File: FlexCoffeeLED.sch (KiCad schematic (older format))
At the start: 29 parts, among them IC1 LM75BDP,118, IC2 PIC16F18426-I_ST, IC3 LM75BDP,118, IC4 LM75BDP,118, J1 Conn_01x05_Male, J2 Conn_01x03_Male, J3 Conn_01x03_Male

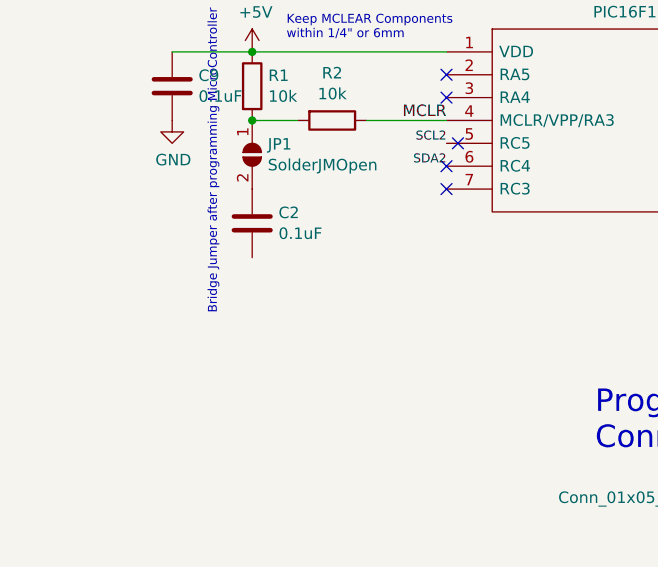
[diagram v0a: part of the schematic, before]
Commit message: Added .git attributes Routed New PCB Design Passed DRC.
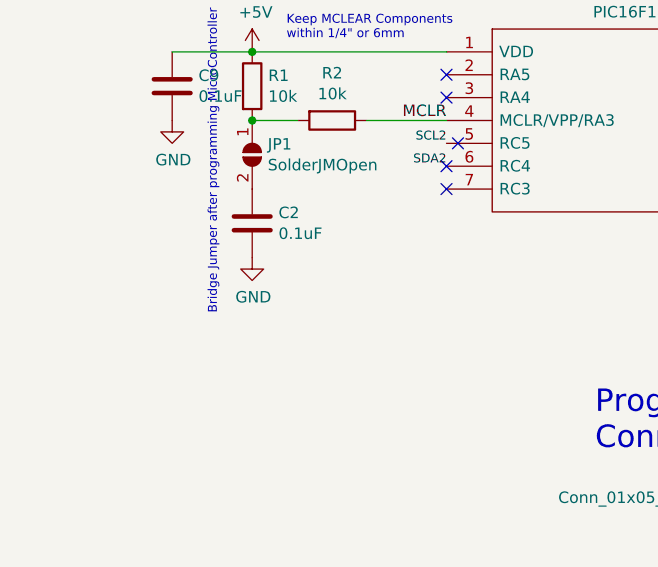
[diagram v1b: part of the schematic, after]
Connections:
- net GND: now also C2.2
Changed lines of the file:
@@
 $EndComp
 $Comp
-L power:+5V #PWR0102
+L power:+5V #PWR?
 U 1 1 5CAA0C63
 P 1650 1100
-F 0 "#PWR0102" H 1650 950 50  0001 C CNN
+F 0 "#PWR?" H 1650 950 50  0001 C CNN
 F 1 "+5V" H 1665 1273 50  0000 C CNN
 F 2 "" H 1650 1100 50  0001 C CNN
@@
 $EndComp
 $Comp
-L power:+5V #PWR0103
+L power:+5V #PWR?
 U 1 1 5CAA255E
 P 2800 1200
-F 0 "#PWR0103" H 2800 1050 50  0001 C CNN
+F 0 "#PWR?" H 2800 1050 50  0001 C CNN
 F 1 "+5V" H 2815 1373 50  0000 C CNN
 F 2 "" H 2800 1200 50  0001 C CNN
@@
 	2800 1350 2800 1200
 $Comp
-L power:GND #PWR0107
+L power:GND #PWR?
 U 1 1 5CAA5599
 P 2450 1450
-F 0 "#PWR0107" H 2450 1200 50  0001 C CNN
+F 0 "#PWR?" H 2450 1200 50  0001 C CNN
 F 1 "GND" H 2455 1277 50  0000 C CNN
 F 2 "" H 2450 1450 50  0001 C CNN
@@
 $EndComp
 $Comp
-L power:GND #PWR0108
+L power:GND #PWR?
 U 1 1 5CAA5C01
 P 3600 1450
-F 0 "#PWR0108" H 3600 1200 50  0001 C CNN
+F 0 "#PWR?" H 3600 1200 50  0001 C CNN
 F 1 "GND" H 3605 1277 50  0000 C CNN
 F 2 "" H 3600 1450 50  0001 C CNN
@@
 SDA_5V
 $Comp
-L power:GND #PWR0111
+L power:GND #PWR?
 U 1 1 5CAACCDF
 P 5150 4250
-F 0 "#PWR0111" H 5150 4000 50  0001 C CNN
+F 0 "#PWR?" H 5150 4000 50  0001 C CNN
 F 1 "GND" H 5155 4077 50  0000 C CNN
 F 2 "" H 5150 4250 50  0001 C CNN
@@
 PGC
 $Comp
-L power:GND #PWR0112
+L power:GND #PWR?
 U 1 1 5CAB3C4D
 P 4250 6550
-F 0 "#PWR0112" H 4250 6300 50  0001 C CNN
+F 0 "#PWR?" H 4250 6300 50  0001 C CNN
 F 1 "GND" H 4255 6377 50  0000 C CNN
 F 2 "" H 4250 6550 50  0001 C CNN
@@
 $EndComp
 $Comp
-L power:+5V #PWR0113
+L power:+5V #PWR?
 U 1 1 5CAB40F3
 P 4250 6300
-F 0 "#PWR0113" H 4250 6150 50  0001 C CNN
+F 0 "#PWR?" H 4250 6150 50  0001 C CNN
 F 1 "+5V" H 4265 6473 50  0000 C CNN
 F 2 "" H 4250 6300 50  0001 C CNN
@@
 	2750 1450 2800 1450
 $Comp
-L power:GND #PWR0118
+L power:GND #PWR?
 U 1 1 5CAE2ED7
 P 2750 1750
-F 0 "#PWR0118" H 2750 1500 50  0001 C CNN
+F 0 "#PWR?" H 2750 1500 50  0001 C CNN
 F 1 "GND" H 2755 1577 50  0000 C CNN
 F 2 "" H 2750 1750 50  0001 C CNN
@@
 $EndComp
 $Comp
-L power:GND #PWR0120
+L power:GND #PWR?
 U 1 1 5CAE8A3F
 P 1550 1750
-F 0 "#PWR0120" H 1550 1500 50  0001 C CNN
+F 0 "#PWR?" H 1550 1500 50  0001 C CNN
 F 1 "GND" H 1555 1577 50  0000 C CNN
 F 2 "" H 1550 1750 50  0001 C CNN
@@
 $EndComp
 $Comp
-L power:GND #PWR0122
+L power:GND #PWR?
 U 1 1 5CB06AB4
 P 1600 4550
-F 0 "#PWR0122" H 1600 4300 50  0001 C CNN
+F 0 "#PWR?" H 1600 4300 50  0001 C CNN
 F 1 "GND" H 1605 4377 50  0000 C CNN
 F 2 "" H 1600 4550 50  0001 C CNN
@@
 $EndComp
 $Comp
-L power:+5V #PWR0123
+L power:+5V #PWR?
 U 1 1 5CB1B5D7
 P 1950 4250
-F 0 "#PWR0123" H 1950 4100 50  0001 C CNN
+F 0 "#PWR?" H 1950 4100 50  0001 C CNN
 F 1 "+5V" H 1965 4423 50  0000 C CNN
 F 2 "" H 1950 4250 50  0001 C CNN
@@
 $EndComp
 $Comp
-L power:+5V #PWR0101
+L power:+5V #PWR?
 U 1 1 5CBD0BE3
 P 9750 4250
-F 0 "#PWR0101" H 9750 4100 50  0001 C CNN
+F 0 "#PWR?" H 9750 4100 50  0001 C CNN
 F 1 "+5V" H 9765 4423 50  0000 C CNN
 F 2 "" H 9750 4250 50  0001 C CNN
@@
 $EndComp
 $Comp
-L power:GND #PWR0104
+L power:GND #PWR?
 U 1 1 5CBD0BF0
 P 9750 4650
-F 0 "#PWR0104" H 9750 4400 50  0001 C CNN
+F 0 "#PWR?" H 9750 4400 50  0001 C CNN
 F 1 "GND" H 9755 4477 50  0000 C CNN
 F 2 "" H 9750 4650 50  0001 C CNN
@@
 	9050 4350 9750 4350
 $Comp
-L power:+5V #PWR0106
+L power:+5V #PWR?
 U 1 1 5CBD1C72
 P 9750 5050
-F 0 "#PWR0106" H 9750 4900 50  0001 C CNN
+F 0 "#PWR?" H 9750 4900 50  0001 C CNN
 F 1 "+5V" H 9765 5223 50  0000 C CNN
 F 2 "" H 9750 5050 50  0001 C CNN
@@
 $EndComp
 $Comp
-L power:GND #PWR0109
+L power:GND #PWR?
 U 1 1 5CBD1C7F
 P 9750 5450
-F 0 "#PWR0109" H 9750 5200 50  0001 C CNN
+F 0 "#PWR?" H 9750 5200 50  0001 C CNN
 F 1 "GND" H 9755 5277 50  0000 C CNN
 F 2 "" H 9750 5450 50  0001 C CNN
@@
 	9050 5150 9350 5150
 $Comp
-L power:+5V #PWR0114
+L power:+5V #PWR?
 U 1 1 5CBD3265
 P 9750 5850
-F 0 "#PWR0114" H 9750 5700 50  0001 C CNN
+F 0 "#PWR?" H 9750 5700 50  0001 C CNN
 F 1 "+5V" H 9765 6023 50  0000 C CNN
 F 2 "" H 9750 5850 50  0001 C CNN
@@
 $EndComp
 $Comp
-L power:GND #PWR0115
+L power:GND #PWR?
 U 1 1 5CBD3272
 P 9750 6250
-F 0 "#PWR0115" H 9750 6000 50  0001 C CNN
+F 0 "#PWR?" H 9750 6000 50  0001 C CNN
 F 1 "GND" H 9755 6077 50  0000 C CNN
 F 2 "" H 9750 6250 50  0001 C CNN
@@
 Connection ~ 9050 4850
 $Comp
-L power:GND #PWR0116
+L power:GND #PWR?
 U 1 1 5CBDC4A5
 P 9400 4800
-F 0 "#PWR0116" H 9400 4550 50  0001 C CNN
+F 0 "#PWR?" H 9400 4550 50  0001 C CNN
 F 1 "GND" H 9405 4627 50  0000 C CNN
 F 2 "" H 9400 4800 50  0001 C CNN
@@
 	9050 4700 9400 4700
 $Comp
-L power:GND #PWR0117
+L power:GND #PWR?
 U 1 1 5CBDF46A
 P 9400 4000
-F 0 "#PWR0117" H 9400 3750 50  0001 C CNN
+F 0 "#PWR?" H 9400 3750 50  0001 C CNN
 F 1 "GND" H 9405 3827 50  0000 C CNN
 F 2 "" H 9400 4000 50  0001 C CNN
@@
 	9050 3900 9400 3900
 $Comp
-L power:GND #PWR0119
+L power:GND #PWR?
 U 1 1 5CBE0081
 P 9100 6300
-F 0 "#PWR0119" H 9100 6050 50  0001 C CNN
+F 0 "#PWR?" H 9100 6050 50  0001 C CNN
 F 1 "GND" H 9105 6127 50  0000 C CNN
 F 2 "" H 9100 6300 50  0001 C CNN
@@
 	9050 4150 9050 4250
 $Comp
-L power:GND #PWR0121
+L power:GND #PWR?
 U 1 1 5CBED2F8
 P 8050 4350
-F 0 "#PWR0121" H 8050 4100 50  0001 C CNN
+F 0 "#PWR?" H 8050 4100 50  0001 C CNN
 F 1 "GND" H 8055 4177 50  0000 C CNN
 F 2 "" H 8050 4350 50  0001 C CNN
@@
 $EndComp
 $Comp
-L power:GND #PWR0125
+L power:GND #PWR?
 U 1 1 5CBED88D
 P 8050 5150
-F 0 "#PWR0125" H 8050 4900 50  0001 C CNN
+F 0 "#PWR?" H 8050 4900 50  0001 C CNN
 F 1 "GND" H 8055 4977 50  0000 C CNN
 F 2 "" H 8050 5150 50  0001 C CNN
@@
 $EndComp
 $Comp
-L power:GND #PWR0126
+L power:GND #PWR?
 U 1 1 5CBEDD70
 P 8050 5950
-F 0 "#PWR0126" H 8050 5700 50  0001 C CNN
+F 0 "#PWR?" H 8050 5700 50  0001 C CNN
 F 1 "GND" H 8055 5777 50  0000 C CNN
 F 2 "" H 8050 5950 50  0001 C CNN
@@
 $EndComp
 $Comp
-L power:+5V #PWR0127
+L power:+5V #PWR?
 U 1 1 5CC0BCE8
 P 3900 1200
-F 0 "#PWR0127" H 3900 1050 50  0001 C CNN
+F 0 "#PWR?" H 3900 1050 50  0001 C CNN
 F 1 "+5V" H 3915 1373 50  0000 C CNN
 F 2 "" H 3900 1200 50  0001 C CNN
@@
 	3900 1350 3900 1200
 $Comp
-L power:GND #PWR0128
+L power:GND #PWR?
 U 1 1 5CC0BCEF
 P 4700 1450
-F 0 "#PWR0128" H 4700 1200 50  0001 C CNN
+F 0 "#PWR?" H 4700 1200 50  0001 C CNN
 F 1 "GND" H 4705 1277 50  0000 C CNN
 F 2 "" H 4700 1450 50  0001 C CNN
@@
 $EndComp
 $Comp
-L power:GND #PWR0129
+L power:GND #PWR?
 U 1 1 5CC0BCFE
 P 3850 1750
-F 0 "#PWR0129" H 3850 1500 50  0001 C CNN
+F 0 "#PWR?" H 3850 1500 50  0001 C CNN
 F 1 "GND" H 3855 1577 50  0000 C CNN
 F 2 "" H 3850 1750 50  0001 C CNN
@@
 $EndComp
 $Comp
-L power:+5V #PWR0130
+L power:+5V #PWR?
 U 1 1 5CC0E352
 P 5000 1200
-F 0 "#PWR0130" H 5000 1050 50  0001 C CNN
+F 0 "#PWR?" H 5000 1050 50  0001 C CNN
 F 1 "+5V" H 5015 1373 50  0000 C CNN
 F 2 "" H 5000 1200 50  0001 C CNN
@@
 	5000 1350 5000 1200
 $Comp
-L power:GND #PWR0131
+L power:GND #PWR?
 U 1 1 5CC0E359
 P 5800 1450
-F 0 "#PWR0131" H 5800 1200 50  0001 C CNN
+F 0 "#PWR?" H 5800 1200 50  0001 C CNN
 F 1 "GND" H 5805 1277 50  0000 C CNN
 F 2 "" H 5800 1450 50  0001 C CNN
@@
 $EndComp
 $Comp
-L power:GND #PWR0132
+L power:GND #PWR?
 U 1 1 5CC0E368
 P 4950 1750
-F 0 "#PWR0132" H 4950 1500 50  0001 C CNN
+F 0 "#PWR?" H 4950 1500 50  0001 C CNN
 F 1 "GND" H 4955 1577 50  0000 C CNN
 F 2 "" H 4950 1750 50  0001 C CNN
@@
 $EndComp
 $Comp
-L power:+5V #PWR0133
+L power:+5V #PWR?
 U 1 1 5CC107D4
 P 6100 1200
-F 0 "#PWR0133" H 6100 1050 50  0001 C CNN
+F 0 "#PWR?" H 6100 1050 50  0001 C CNN
 F 1 "+5V" H 6115 1373 50  0000 C CNN
 F 2 "" H 6100 1200 50  0001 C CNN
@@
 	6100 1350 6100 1200
 $Comp
-L power:GND #PWR0134
+L power:GND #PWR?
 U 1 1 5CC107DB
 P 6900 1450
-F 0 "#PWR0134" H 6900 1200 50  0001 C CNN
+F 0 "#PWR?" H 6900 1200 50  0001 C CNN
 F 1 "GND" H 6905 1277 50  0000 C CNN
 F 2 "" H 6900 1450 50  0001 C CNN
@@
 $EndComp
 $Comp
-L power:GND #PWR0135
+L power:GND #PWR?
 U 1 1 5CC107EA
 P 6050 1750
-F 0 "#PWR0135" H 6050 1500 50  0001 C CNN
+F 0 "#PWR?" H 6050 1500 50  0001 C CNN
 F 1 "GND" H 6055 1577 50  0000 C CNN
 F 2 "" H 6050 1750 50  0001 C CNN
@@
 $EndComp
 $Comp
-L power:+5V #PWR0136
+L power:+5V #PWR?
 U 1 1 5CC12656
 P 7200 1200
-F 0 "#PWR0136" H 7200 1050 50  0001 C CNN
+F 0 "#PWR?" H 7200 1050 50  0001 C CNN
 F 1 "+5V" H 7215 1373 50  0000 C CNN
 F 2 "" H 7200 1200 50  0001 C CNN
@@
 	7200 1350 7200 1250
 $Comp
-L power:GND #PWR0137
+L power:GND #PWR?
 U 1 1 5CC1265D
 P 8000 1450
-F 0 "#PWR0137" H 8000 1200 50  0001 C CNN
+F 0 "#PWR?" H 8000 1200 50  0001 C CNN
 F 1 "GND" H 8005 1277 50  0000 C CNN
 F 2 "" H 8000 1450 50  0001 C CNN
@@
 $EndComp
 $Comp
-L power:GND #PWR0138
+L power:GND #PWR?
 U 1 1 5CC1266C
 P 7150 1750
-F 0 "#PWR0138" H 7150 1500 50  0001 C CNN
+F 0 "#PWR?" H 7150 1500 50  0001 C CNN
 F 1 "GND" H 7155 1577 50  0000 C CNN
 F 2 "" H 7150 1750 50  0001 C CNN
@@
 Wire Wire Line
 	8250 1300 8250 1350
+$Comp
+L power:GND #PWR?
+U 1 1 5CC40DD0
+P 1950 5150
+F 0 "#PWR?" H 1950 4900 50  0001 C CNN
+F 1 "GND" H 1955 4977 50  0000 C CNN
+F 2 "" H 1950 5150 50  0001 C CNN
+F 3 "" H 1950 5150 50  0001 C CNN
+	1    1950 5150
+	1    0    0    -1
+$EndComp
 $EndSCHEMATC

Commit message: small Changes
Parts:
- C1, C3, C4, C5, C6, C7: value 15pF -> 0.1uF
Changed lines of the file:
@@
 P 2750 1600
 F 0 "C5" H 2865 1646 50  0000 L CNN
-F 1 "15pF" H 2865 1555 50  0000 L CNN
+F 1 "0.1uF" H 2865 1555 50  0000 L CNN
 F 2 "Capacitors_SMD:C_0603" H 2788 1450 50  0001 C CNN
 F 3 "~" H 2750 1600 50  0001 C CNN
@@
 P 1550 1600
 F 0 "C3" H 1665 1646 50  0000 L CNN
-F 1 "15pF" H 1665 1555 50  0000 L CNN
+F 1 "0.1uF" H 1665 1555 50  0000 L CNN
 F 2 "Capacitors_SMD:C_0603" H 1588 1450 50  0001 C CNN
 F 3 "~" H 1550 1600 50  0001 C CNN
@@
 F 5 "1.1" H 8900 3850 50  0001 L CNN "Height"
 F 6 "771-LM75BDP" H 8900 3750 50  0001 L CNN "Mouser Part Number"
-F 7 "" H 8900 3650 50  0001 L CNN "Mouser Price/Stock"
-F 8 "NXP" H 8900 3550 50  0001 L CNN "Manufacturer_Name"
-F 9 "LM75BDP,118" H 8900 3450 50  0001 L CNN "Manufacturer_Part_Number"
+F 7 "NXP" H 8900 3550 50  0001 L CNN "Manufacturer_Name"
+F 8 "LM75BDP,118" H 8900 3450 50  0001 L CNN "Manufacturer_Part_Number"
 	1    8050 4050
 	1    0    0    -1
@@
 F 5 "1.1" H 8900 4650 50  0001 L CNN "Height"
 F 6 "771-LM75BDP" H 8900 4550 50  0001 L CNN "Mouser Part Number"
-F 7 "" H 8900 4450 50  0001 L CNN "Mouser Price/Stock"
-F 8 "NXP" H 8900 4350 50  0001 L CNN "Manufacturer_Name"
-F 9 "LM75BDP,118" H 8900 4250 50  0001 L CNN "Manufacturer_Part_Number"
+F 7 "NXP" H 8900 4350 50  0001 L CNN "Manufacturer_Name"
+F 8 "LM75BDP,118" H 8900 4250 50  0001 L CNN "Manufacturer_Part_Number"
 	1    8050 4850
 	1    0    0    -1
@@
 F 5 "1.1" H 8900 5450 50  0001 L CNN "Height"
 F 6 "771-LM75BDP" H 8900 5350 50  0001 L CNN "Mouser Part Number"
-F 7 "" H 8900 5250 50  0001 L CNN "Mouser Price/Stock"
-F 8 "NXP" H 8900 5150 50  0001 L CNN "Manufacturer_Name"
-F 9 "LM75BDP,118" H 8900 5050 50  0001 L CNN "Manufacturer_Part_Number"
+F 7 "NXP" H 8900 5150 50  0001 L CNN "Manufacturer_Name"
+F 8 "LM75BDP,118" H 8900 5050 50  0001 L CNN "Manufacturer_Part_Number"
 	1    8050 5650
 	1    0    0    -1
@@
 P 3850 1600
 F 0 "C1" H 3965 1646 50  0000 L CNN
-F 1 "15pF" H 3965 1555 50  0000 L CNN
+F 1 "0.1uF" H 3965 1555 50  0000 L CNN
 F 2 "Capacitors_SMD:C_0603" H 3888 1450 50  0001 C CNN
 F 3 "~" H 3850 1600 50  0001 C CNN
@@
 P 4950 1600
 F 0 "C4" H 5065 1646 50  0000 L CNN
-F 1 "15pF" H 5065 1555 50  0000 L CNN
+F 1 "0.1uF" H 5065 1555 50  0000 L CNN
 F 2 "Capacitors_SMD:C_0603" H 4988 1450 50  0001 C CNN
 F 3 "~" H 4950 1600 50  0001 C CNN
@@
 P 6050 1600
 F 0 "C6" H 6165 1646 50  0000 L CNN
-F 1 "15pF" H 6165 1555 50  0000 L CNN
+F 1 "0.1uF" H 6165 1555 50  0000 L CNN
 F 2 "Capacitors_SMD:C_0603" H 6088 1450 50  0001 C CNN
 F 3 "~" H 6050 1600 50  0001 C CNN
@@
 P 7150 1600
 F 0 "C7" H 7265 1646 50  0000 L CNN
-F 1 "15pF" H 7265 1555 50  0000 L CNN
+F 1 "0.1uF" H 7265 1555 50  0000 L CNN
 F 2 "Capacitors_SMD:C_0603" H 7188 1450 50  0001 C CNN
 F 3 "~" H 7150 1600 50  0001 C CNN
@@
 F 4 "8-bit Microcontrollers - MCU 28KB, 2KB RAM, 2xPWMs, Comparator, DAC, 12-bit ADCC, CWG,  EUSART, SPI/I2C" H 4550 4150 50  0001 L CNN "Description"
 F 5 "1.2" H 4550 4050 50  0001 L CNN "Height"
-F 6 "" H 4550 3950 50  0001 L CNN "Mouser Part Number"
-F 7 "" H 4550 3850 50  0001 L CNN "Mouser Price/Stock"
-F 8 "Microchip" H 4550 3750 50  0001 L CNN "Manufacturer_Name"
-F 9 "PIC16F18426-I/ST" H 4550 3650 50  0001 L CNN "Manufacturer_Part_Number"
+F 6 "Microchip" H 4550 3750 50  0001 L CNN "Manufacturer_Name"
+F 7 "PIC16F18426-I/ST" H 4550 3650 50  0001 L CNN "Manufacturer_Part_Number"
 	1    2800 4250
 	1    0    0    -1
